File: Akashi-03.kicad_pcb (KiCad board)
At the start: 2 copper layers, 71.1 x 67.3 mm, 33 parts, among them CN10 PPPC192LFBN-RC, CN7 PPPC192LFBN-RC, SW1 PEC11R-4220F-S0024

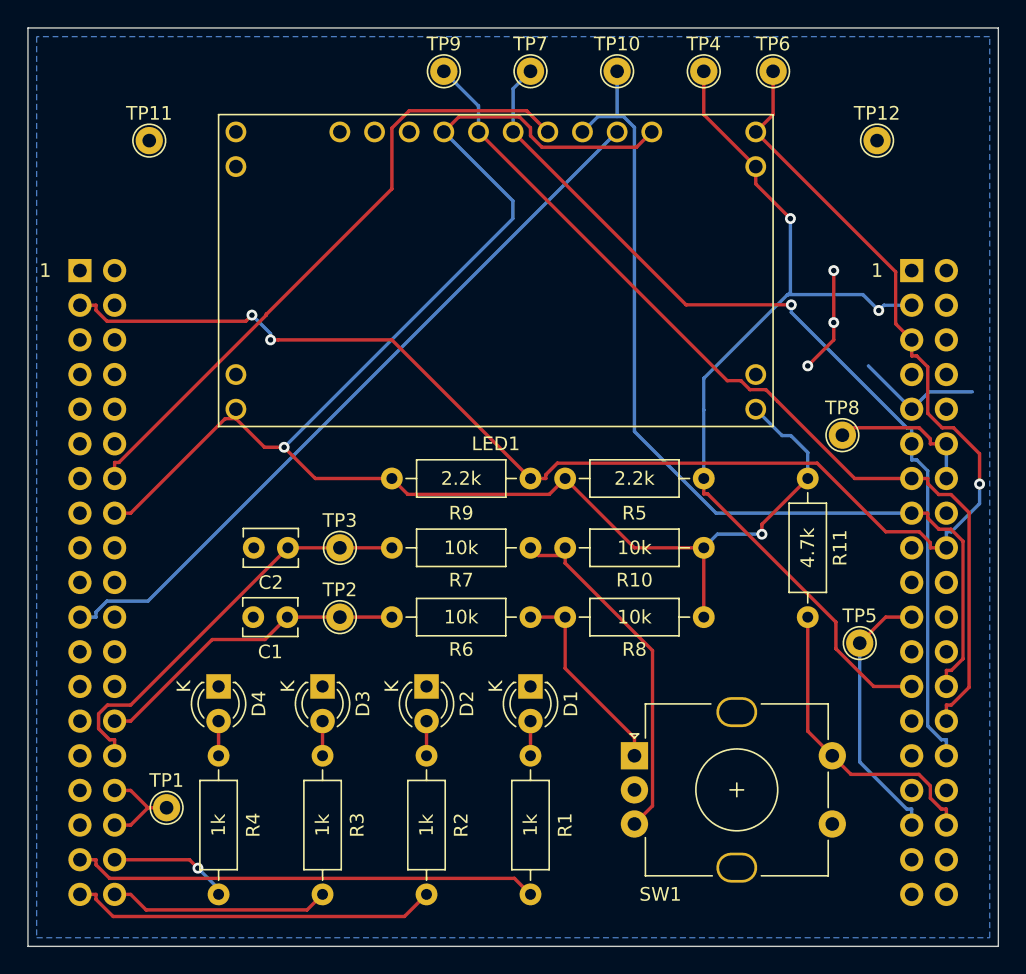
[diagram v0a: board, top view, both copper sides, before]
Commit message: Complete the schematics.
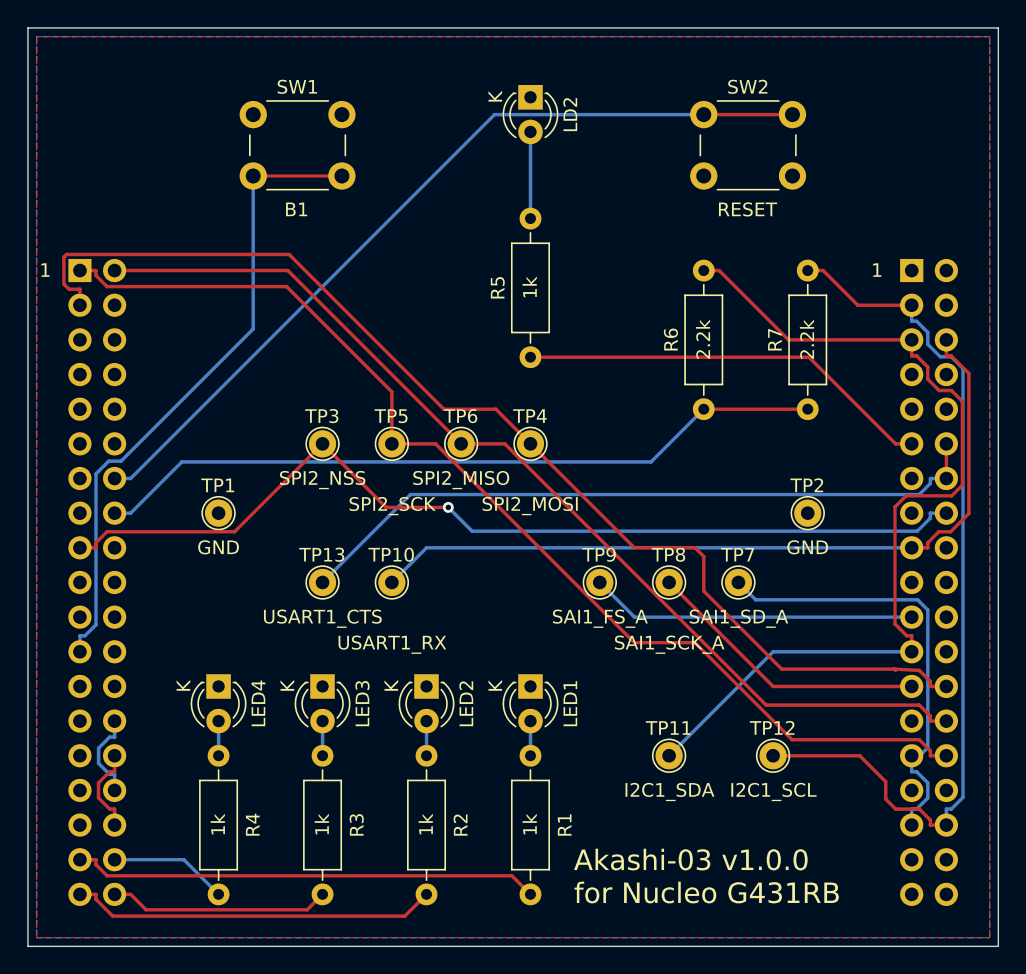
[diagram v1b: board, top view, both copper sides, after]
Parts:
- removed C1, C2: 0.01u, Capacitor_THT:C_Disc_D3.8mm_W2.6mm_P2.50mm
- removed the LED1 at (130.8, 50.8)
- removed R10, R8: 10k, Resistor_THT:R_Axial_DIN0207_L6.3mm_D2.5mm_P10.16mm_Horizontal
- removed R11: 4.7k, Resistor_THT:R_Axial_DIN0207_L6.3mm_D2.5mm_P10.16mm_Horizontal
- removed R9: 2.2k, Resistor_THT:R_Axial_DIN0207_L6.3mm_D2.5mm_P10.16mm_Horizontal
- removed the TP1 at (125.7, 100.3)
- removed the TP2 at (138.4, 86.4)
- added LD2: LED, LED_THT:LED_D3.0mm_Clear, F.Cu at (152.4, 48.3)
- added SW2: SW_Push, Button_Switch_THT:SW_PUSH_6mm_H5mm, F.Cu at (165.1, 49.5)
- added TP11: GND, TestPoint:TestPoint_THTPad_D2.0mm_Drill1.0mm, F.Cu at (162.6, 96.5)
- added TP12: GND, TestPoint:TestPoint_THTPad_D2.0mm_Drill1.0mm, F.Cu at (170.2, 96.5)
- added TP13: GND, TestPoint:TestPoint_THTPad_D2.0mm_Drill1.0mm, F.Cu at (137.2, 83.8)
- R5: value 2.2k -> 1k
- R6, R7: value 10k -> 2.2k
- SW1: value PEC11R-4220F-S0024 -> SW_Push; footprint Rotary_Encoder:RotaryEncoder_Alps_EC12E-Switch_Vertical_H20mm_CircularMountingHoles -> Button_Switch_THT:SW_PUSH_6mm_H5mm
- TP10: value MOSI -> GND
- TP3: value CH2 -> GND
- TP4: value SCL -> GND
- TP5: value TX -> GND
- TP6: value SDA -> GND
- TP7: value SCK -> GND
- TP8: value RTS -> GND
- TP9: value MISO -> GND
- moved SW1 54.7 mm to (132.1, 49.5)
- moved TP10 40.9 mm to (142.2, 83.8)
- moved TP7 40.4 mm to (167.6, 83.8)
- moved TP9 39.2 mm to (157.5, 83.8)
- moved TP5 37.3 mm to (142.2, 73.7)
- moved TP6 35.6 mm to (147.3, 73.7)
- moved TP4 30.1 mm to (152.4, 73.7)
- moved TP1 27.8 mm to (129.5, 78.7)
- moved TP2 27.8 mm to (172.7, 78.7)
- moved R7 22.7 mm to (172.7, 71.1), turned to 90 degrees
- moved R6 19.8 mm to (165.1, 71.1), turned to 90 degrees
- moved TP8 16.7 mm to (162.6, 83.8)
- moved R5 9.25 mm to (152.4, 67.3), turned to 90 degrees
- moved TP3 7.73 mm to (137.2, 73.7)
- renumbered CN7 to CN1, CN10 to CN2, D1 to LED1, D2 to LED2, D3 to LED3, D4 to LED4, TP11 to TP1, TP12 to TP2
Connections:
- CN1 pad 1: Net-(CN7-Pad1) -> /SPI2_SCK
- CN1 pad 17: Net-(CN7-Pad17) -> /SPI2_NSS
- CN1 pad 2: Net-(CN7-Pad2) -> /SPI2_MISO
- CN1 pad 21: /nLEDCS -> Net-(CN1-Pad21)
- CN1 pad 23: Net-(CN7-Pad23) -> /B1
- CN1 pad 28: /TIM2_CH1 -> /CH1_CTL
- CN1 pad 3: /I2C1_SDA -> /SPI2_MOSI
- CN1 pad 30: /TIM2_CH2 -> /CH2_CTL
- CN1 pad 32: /SPI1_NSS -> /CH1_CTL
- CN1 pad 34: /SPI1_NSS -> /CH2_CTL
- CN2 pad 11: /SPI1_SCK -> /LD2
- CN2 pad 13: /SPI1_MISO -> Net-(CN2-Pad13)
- CN2 pad 15: /SPI1_MOSI -> Net-(CN2-Pad15)
- CN2 pad 16: Net-(CN10-Pad16) -> /SPI2_NSS
- CN2 pad 17: Net-(CN10-Pad17) -> /USART1_RX
- CN2 pad 18: /I2C1_SDA -> Net-(CN2-Pad18)
- CN2 pad 21: /UART1_TX -> /SAI1_FS_A
- CN2 pad 23: Net-(CN10-Pad23) -> /I2C1_SDA
- CN2 pad 25: /I2C1_SCL -> /SAI1_SCK_A
- CN2 pad 26: /SPI1_MOSI -> /SPI2_MOSI
- CN2 pad 28: /SPI1_MISO -> /SPI2_MISO
- CN2 pad 29: Net-(CN10-Pad29) -> /SAI1_SD_A
- CN2 pad 30: /SPI1_SCK -> /SPI2_SCK
- CN2 pad 33: /UART1_TX -> /SAI1_SD_A
- CN2 pad 34: /SW1 -> /I2C1_SCL
- CN2 pad 6: Net-(CN10-Pad6) -> /USART1_RX
- R5 pad 1: +3V3 -> /LD2
- R5 pad 2: /I2C1_SCL -> Net-(LD2-Pad2)
- R6 pad 1: Net-(R6-Pad1) -> +3V3
- R6 pad 2: /TIM2_CH1 -> /I2C1_SDA
- R7 pad 1: Net-(R10-Pad2) -> +3V3
- R7 pad 2: /TIM2_CH2 -> /I2C1_SCL
- TP10 pad 1: /SPI1_MOSI -> /USART1_RX
- TP3 pad 1: /TIM2_CH2 -> /SPI2_NSS
- TP4 pad 1: /I2C1_SCL -> /SPI2_MOSI
- TP5 pad 1: /UART1_TX -> /SPI2_SCK
- TP6 pad 1: /I2C1_SDA -> /SPI2_MISO
- TP7 pad 1: /SPI1_SCK -> /SAI1_SD_A
- TP8 pad 1: /USART1_CTS -> /SAI1_SCK_A
- TP9 pad 1: /SPI1_MISO -> /SAI1_FS_A
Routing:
- net /SPI2_MOSI: track 0.00 -> 84.2 mm
- net /SPI2_SCK: track 0.00 -> 80.9 mm
- net /SPI2_MISO: track 0.00 -> 74.9 mm
- net /SPI2_NSS: track 0.00 -> 70.3 mm, vias 0 -> 1
- net +3V3: track 123.6 -> 54.0 mm, vias 2 -> 0
- net /SPI1_MISO: track 69.4 -> 0.00 mm
- net /SPI1_MOSI: track 69.2 -> 0.00 mm
- net /SPI1_SCK: track 69.0 -> 0.00 mm, vias 1 -> 0
- net /USART1_RX: track 0.00 -> 58.2 mm
- net /nLEDCS: track 54.3 -> 0.00 mm
- net /I2C1_SDA: track 116.9 -> 68.1 mm, vias 3 -> 0
- net /B1: track 0.00 -> 47.4 mm
- net /USART1_CTS: track 11.1 -> 51.6 mm
- net /SAI1_SD_A: track 0.00 -> 33.0 mm
- net /LD2: track 0.00 -> 30.6 mm
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- added copper zone on F.Cu, net GND
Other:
- board text added: "(C) Seiichi Horie 2020 https://github.com/suikan4github/Akashi-03"
- board text added: "Akashi-03 v1.0.0 for Nucleo G431RB"
- board text added: "B1"
- board text added: "GND"
- board text added: "I2C1_SCL"
- board text added: "I2C1_SDA"
- board text added: "RESET"
- board text added: "SAI1_FS_A"
- board text added: "SAI1_SCK_A"
- board text added: "SAI1_SD_A"
- board text added: "SPI2_MISO"
- board text added: "SPI2_MOSI"
- board text added: "SPI2_NSS"
- board text added: "SPI2_SCK"
- board text added: "USART1_CTS"
- board text added: "USART1_RX"
- board text removed: "Akashi-01 v1.0.4 A Murasaki JIG for Nucleo 64 (C) Seiichi Horie 2019 https://github.com/suikan4github/Akashi-01"
